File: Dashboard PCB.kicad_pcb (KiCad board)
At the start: 2 copper layers, 62 parts, among them J1 Controls_Leader_Export_02x06, J3 INDICATOR_SWITCH_OUT, J4 FAN_CTRL_01x02, J5 Horn_In_01x02, J6 Horn_Out_01x02

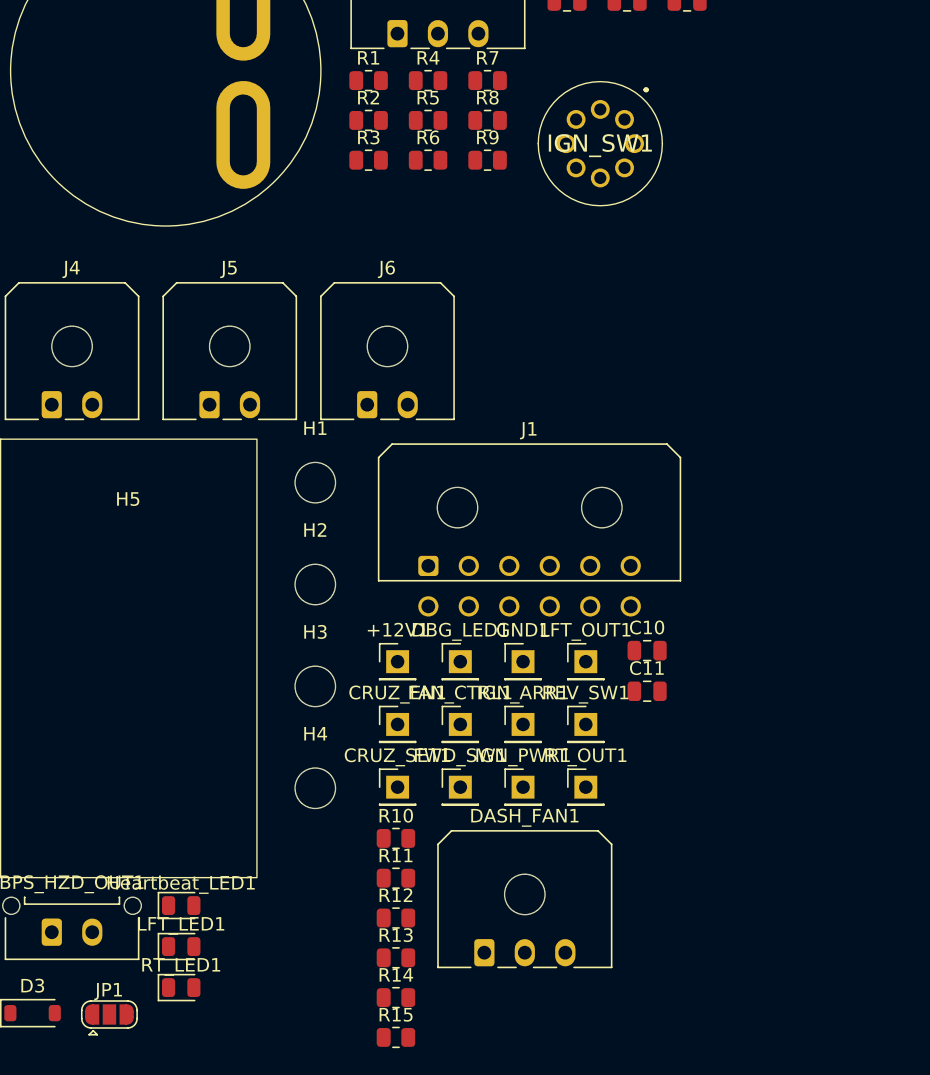
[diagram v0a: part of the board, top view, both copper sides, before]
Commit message: Fixed fan and rot switch
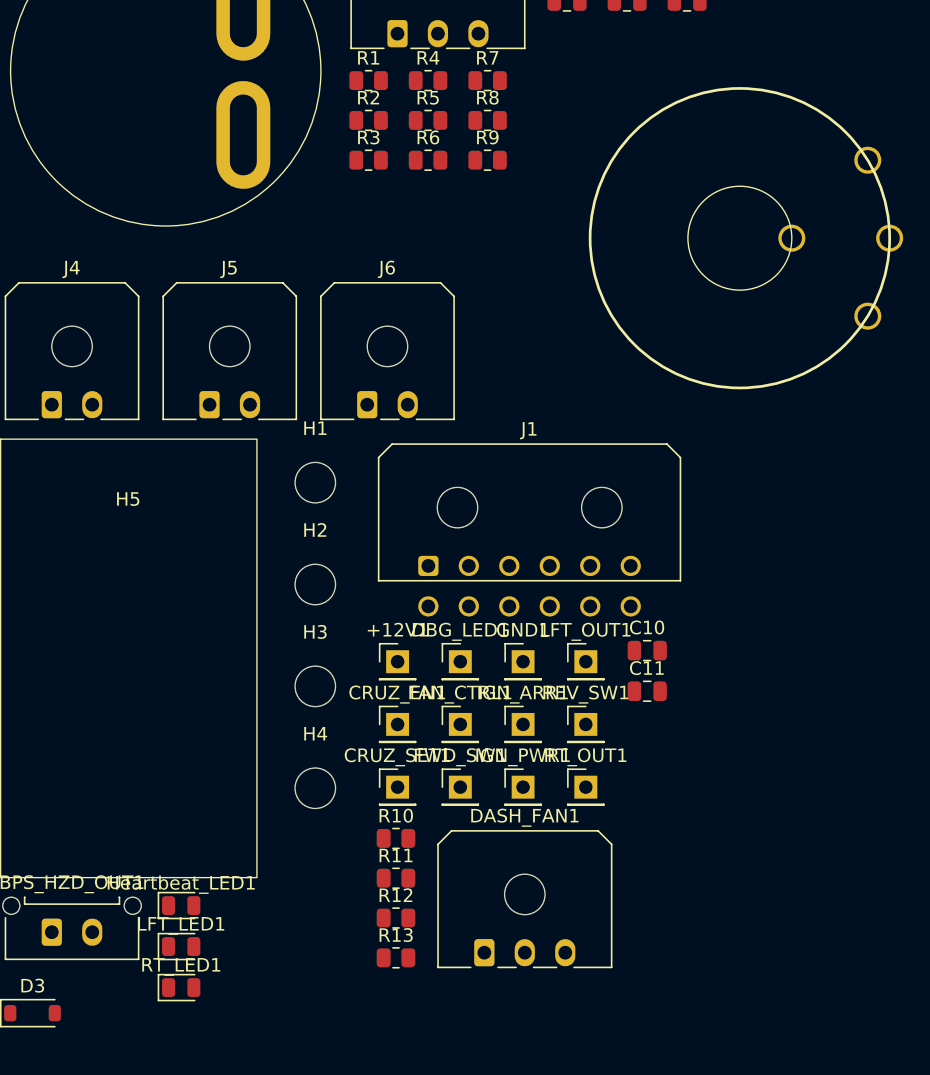
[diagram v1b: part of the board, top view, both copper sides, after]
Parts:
- removed JP1: Jumper_3_Open, Jumper:SolderJumper-3_P1.3mm_Open_RoundedPad1.0x1.5mm
- removed R14: 1.8k, Resistor_SMD:R_0805_2012Metric
- removed R15: 680, Resistor_SMD:R_0805_2012Metric
- DASH_FAN1: value DASHBOARD_FAN_12V+PWM -> DASHBOARD_FAN_12V
- IGN_SW1: footprint switched:SW_ROT_3POS -> switched:SW_3POS_ROT
- moved IGN_SW1 12.3 mm to (72.0, 67.2)
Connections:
- D3 pad 1: +12V -> /FAN+
- D3 pad 2: GND -> /FAN-
- DASH_FAN1 pad 1: +12V -> /FAN+
- DASH_FAN1 pad 2: /FAN_CTRL -> /FAN-
- DASH_FAN1 pad 3: GND -> unconnected-(DASH_FAN1-Pin_3-Pad3)
- FAN_CTRL1 pad 1: /FAN_CTRL -> /FAN+
- IGN_SW1 pad 1: unconnected-(IGN_SW1-Pad1) -> +12V
- J4 pad 1: /FAN_PWM -> /FAN+
- J4 pad 2: GND -> /FAN-

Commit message: Preliminary PCB layout
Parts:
- moved H2 216.3 mm to (246.9, 28.0)
- moved H4 209.4 mm to (246.9, 143.6)
- moved H5 189.2 mm to (215.8, 104.4)
- moved IGN_ARR1 160.8 mm to (212.2, 65.2)
- moved R5 152.7 mm to (199.7, 82.3), turned to 90 degrees
- moved RT_LED1 147.4 mm to (160.8, 53.6)
- moved CRUZ_SET_SW1 146.9 mm to (169.3, 99.7), turned to -90 degrees
- moved R6 136.0 mm to (183.3, 82.5), turned to 90 degrees
- moved LFT_LED1 136.0 mm to (149.4, 53.6), turned to 180 degrees
- moved C5 135.4 mm to (194.2, 82.5), turned to -90 degrees
- moved R11 132.8 mm to (164.8, 54.3), turned to 90 degrees
- moved R8 131.7 mm to (172.0, 115.6), turned to -90 degrees
- moved C6 128.8 mm to (188.2, 82.7), turned to -90 degrees
- moved IGN_PWR1 125.8 mm to (174.2, 65.1)
- moved CRUZ_EN_SW1 124.2 mm to (131.8, 99.5), turned to -90 degrees
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
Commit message: Preliminary schematic
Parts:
- moved R13 140.9 mm to (228.6, 125.1)
- moved BPS_HZD_OUT1 140.7 mm to (227.1, 131.9)
- moved H5 108.7 mm to (116.7, 59.8)
- moved C2 54.9 mm to (69.7, 122.6), turned to 180 degrees
- moved J3 54.6 mm to (76.0, 128.2), turned to 180 degrees
- moved R2 50.8 mm to (69.7, 117.8), turned to 0 degrees
- moved C1 47.3 mm to (76.9, 122.7), turned to 180 degrees
- moved J6 44.9 mm to (89.1, 128.2), turned to 180 degrees
- moved R1 42.5 mm to (77.0, 118.1), turned to 0 degrees
- moved C7 36.1 mm to (149.3, 74.3)
- moved D1 36.1 mm to (148.9, 65.2)
- moved HZD_SW1 36.1 mm to (161.4, 72.2)
- moved R7 36.1 mm to (149.4, 69.2)
- moved D2 36.1 mm to (148.7, 79.6)
- moved H1 35.9 mm to (53.5, 42.6)
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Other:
- board text added: "Controls Export"
- board text added: "Fan Ctrl"
- board text added: "Horn In"
- board text added: "Horn Out"
- board text added: "Indicator Sw Out"

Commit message: r
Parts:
- moved H2 0.82 mm to (243.6, 42.6)
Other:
- board outline added: 200 x 100 mm
- board text added: "20cm x 10cm"
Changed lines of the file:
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@@
 		(tags "capacitor")
 		(property "Reference" "C2"
-			(at 0 -1.68 360)
+			(at 0 -1.68 0)
 			(layer "F.SilkS")
 			(effects
@@
 		)
 		(property "Value" "5uF"
-			(at 0 1.68 360)
+			(at 0 1.68 0)
 			(layer "F.Fab")
 			(effects
@@
 		(tags "connector Molex Micro-Fit_3.0 top entry")
 		(property "Reference" "J6"
-			(at 1.5 -8.1 360)
+			(at 1.5 -8.1 0)
 			(layer "F.SilkS")
 			(effects
@@
 		)
 		(property "Value" "Horn_Out_01x02"
-			(at 1.5 3.22 360)
+			(at 1.5 3.22 0)
 			(layer "F.Fab")
 			(hide yes)
@@
 		(tags "resistor")
 		(property "Reference" "R2"
-			(at 0 -1.65 360)
+			(at 0 -1.65 0)
 			(layer "F.SilkS")
 			(effects
@@
 		)
 		(property "Value" "10k"
-			(at 0 1.65 360)
+			(at 0 1.65 0)
 			(layer "F.Fab")
 			(effects
@@
 		(tags "resistor")
 		(property "Reference" "R13"
-			(at 0 -1.65 360)
+			(at 0 -1.65 0)
 			(layer "F.SilkS")
 			(effects
@@
 		)
 		(property "Value" "HZD_RES_VAL"
-			(at 0 1.65 360)
+			(at 0 1.65 0)
 			(layer "F.Fab")
 			(effects
@@
 		)
 		(fp_text user "${REFERENCE}"
-			(at 0 0 360)
+			(at 0 0 0)
 			(layer "F.Fab")
 			(effects
@@
 	(footprint "MountingHole:MountingHole_3mm"
 		(layer "F.Cu")
-		(at 243.8 41.8)
+		(at 243.6 42.6)
 		(descr "Mounting Hole 3mm, no annular")
 		(tags "mounting hole 3mm no annular")
@@
 		(tags "capacitor")
 		(property "Reference" "C1"
-			(at 0 -1.68 360)
+			(at 0 -1.68 0)
 			(layer "F.SilkS")
 			(effects
@@
 		)
 		(property "Value" "5uF"
-			(at 0 1.68 360)
+			(at 0 1.68 0)
 			(layer "F.Fab")
 			(effects
@@
 		(tags "connector Molex Micro-Fit_3.0 top entry")
 		(property "Reference" "J3"
-			(at 2.6 -8.1 360)
+			(at 2.6 -8.1 0)
 			(layer "F.SilkS")
 			(effects
@@
 		)
 		(property "Value" "INDICATOR_SWITCH_OUT"
-			(at 3 3.22 360)
+			(at 3 3.22 0)
 			(layer "F.Fab")
 			(hide yes)
@@
 		(tags "connector Molex Micro-Fit_3.0 vertical")
 		(property "Reference" "BPS_HZD_OUT1"
-			(at 1.5 -3.67 360)
+			(at 1.5 -3.67 0)
 			(layer "F.SilkS")
 			(effects
@@
 		)
 		(property "Value" "BPS_HAZARD_LIGHT"
-			(at 1.5 4.5 360)
+			(at 1.5 4.5 0)
 			(layer "F.Fab")
 			(effects
@@
 		)
 		(fp_text user "${REFERENCE}"
-			(at 1.5 1.2 360)
+			(at 1.5 1.2 0)
 			(layer "F.Fab")
 			(effects
@@
 		(tags "resistor")
 		(property "Reference" "R1"
-			(at 0 -1.65 360)
+			(at 0 -1.65 0)
 			(layer "F.SilkS")
 			(effects
@@
 		)
 		(property "Value" "10k"
-			(at 0 1.65 360)
+			(at 0 1.65 0)
 			(layer "F.Fab")
 			(effects
@@
 		)
 		(property "Value" "TestPoint"
-			(at 0 2.33 360)
+			(at 0 2.33 0)
 			(layer "F.Fab")
 			(hide yes)
@@
 		)
 		(fill none)
-		(layer "F.Cu")
+		(layer "Edge.Cuts")
+	)
+	(gr_text "20cm x 10cm"
+		(at 45.9 33.4 0)
+		(layer "F.SilkS")
+		(effects
+			(font
+				(size 2 2)
+				(thickness 0.1)
+			)
+			(justify left bottom)
+		)
 	)
 	(gr_text "Controls Export"

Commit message: Changed layout, added 3d models
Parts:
- added J2: CAN, Connector_Molex:Molex_Micro-Fit_3.0_43045-0600_2x03_P3.00mm_Horizontal, B.Cu at (74.0, 104.0)
- added J7: CAN, Connector_Molex:Molex_Micro-Fit_3.0_43045-0600_2x03_P3.00mm_Horizontal, B.Cu at (86.0, 133.0)
- +12V1, BPS_HZD_OUT1, C1, C10, C11, C2, C3, C4, C5, C6, C7, C8, C9, CRUZ_EN1, CRUZ_SET1, D1, D2, D3, DASH_FAN1, DBG_LED1, FAN_CTRL1, FWD_SW1, GND1, Heartbeat_LED1, IGN_ARR1, IGN_PWR1, J1, J3, J4, J5, J6, LFT_OUT1, R1, R10, R11, R12, R13, R2, R3, R4, R5, R6, R7, R8, R9, REV_SW1, RT_OUT1: moved to B.Cu
- CRUZ_EN_SW1, CRUZ_SET_SW1: footprint switched:SW_Butt_) -> Button_Switch_THT:SW_PUSH_6mm
- GR_SW1: footprint switched:SW_100_SP3T-Vertical -> switched:3posSlideToggle
- moved IGN_ARR1 133.0 mm to (93.0, 61.0), turned to 180 degrees
- moved CRUZ_SET1 113.8 mm to (117.0, 49.0), turned to 180 degrees
- moved IGN_PWR1 95.7 mm to (93.0, 55.0), turned to 180 degrees
- moved CRUZ_EN1 86.3 mm to (117.0, 55.0), turned to 180 degrees
- moved FAN_CTRL1 73.3 mm to (101.0, 61.0), turned to -90 degrees
- moved RT_OUT1 56.6 mm to (117.0, 61.0), turned to 180 degrees
- moved LFT_OUT1 50.2 mm to (101.0, 49.0), turned to 180 degrees
- moved REV_SW1 48.7 mm to (109.0, 55.0), turned to 180 degrees
- moved R7 41.6 mm to (189.0, 82.0), turned to 90 degrees
- moved D2 40.4 mm to (189.0, 77.0), turned to -90 degrees
- moved R2 38.9 mm to (107.5, 127.0)
- moved R10 38.4 mm to (189.0, 61.0)
- moved C2 37.8 mm to (107.5, 123.0)
- moved FWD_SW1 37.1 mm to (109.0, 61.0), turned to 180 degrees
- moved LFT_LED1 36.7 mm to (192.0, 58.0)
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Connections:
- BPS_HZD_OUT1 pad 2: GND -> /BPS_HZD
- GR_SW1 pad 1: /FWD_SW -> +12V
- GR_SW1 pad 2: +12V -> /FWD_SW
- GR_SW1 pad 3: /REV_SW -> (no net)
- Heartbeat_LED1 pad 1: GND -> /DBG_LED
- R12 pad 1: /DBG_LED -> +12V
- R13 pad 1: /BPS_HZD -> +12V
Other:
- outline, holes or cut-outs redrawn
- board text added: "Approx 3d model"
- board text added: "Placeholder 3d model"

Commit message: Some extra stuff and things
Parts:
- HZD_SW1: footprint switched:SW_HAZARD -> switched:Toggle
- moved HZD_SW1 2.50 mm to (180.0, 78.5)
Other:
- outline, holes or cut-outs redrawn
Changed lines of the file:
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@@
 		(tags "LED")
 		(property "Reference" "LFT_LED1"
-			(at 0 2 360)
+			(at 0 2 0)
 			(layer "F.SilkS")
 			(effects
@@
 		)
 		(property "Value" "SMD_0805"
-			(at 0 1.65 360)
+			(at 0 1.65 0)
 			(layer "F.Fab")
 			(hide yes)
@@
 		)
 	)
-	(footprint "switched:SW_HAZARD"
+	(footprint "switched:Toggle"
 		(layer "F.Cu")
-		(at 180 81)
+		(at 180 78.5)
 		(property "Reference" "HZD_SW1"
-			(at 0.21 -14.17 0)
+			(at -0.16 7 0)
+			(unlocked yes)
 			(layer "F.SilkS")
-			(hide yes)
 			(effects
 				(font
 					(size 1 1)
-					(thickness 0.15)
+					(thickness 0.1)
 				)
 			)
 		)
 		(property "Value" "HAZARD_SWITCH_12V"
-			(at -0.03 13.54 0)
+			(at 0 9 0)
+			(unlocked yes)
 			(layer "F.Fab")
-			(hide yes)
 			(effects
 				(font
@@
 			)
 		)
-		(property "Footprint" "switched:SW_HAZARD"
-			(at -0.34 -0.31 0)
+		(property "Footprint" "switched:Toggle"
+			(at -0.16 9.85 0)
+			(unlocked yes)
 			(layer "F.Fab")
 			(hide yes)
 			(effects
 				(font
-					(size 1.27 1.27)
+					(size 1 1)
 					(thickness 0.15)
 				)
@@
 		)
 		(property "Datasheet" "https://www.digikey.com/en/products/detail/switch-components/TE1-1A-DC-1-AL/11493057"
-			(at -0.34 -0.31 0)
+			(at -0.16 9.85 0)
+			(unlocked yes)
 			(layer "F.Fab")
 			(hide yes)
 			(effects
 				(font
-					(size 1.27 1.27)
+					(size 1 1)
 					(thickness 0.15)
 				)
@@
 		)
 		(property "Description" "Single Pole Single Throw (SPST) switch"
-			(at -0.34 -0.31 0)
+			(at -0.16 9.85 0)
+			(unlocked yes)
 			(layer "F.Fab")
 			(hide yes)
 			(effects
 				(font
-					(size 1.27 1.27)
+					(size 1 1)
 					(thickness 0.15)
 				)
@@
 		(attr through_hole)
 		(fp_rect
-			(start -7 -12.19)
-			(end 7 12.21)
+			(start -5 -5)
+			(end 5 5)
 			(stroke
 				(width 0.1)
@@
 			(layer "F.SilkS")
 		)
-		(fp_circle
-			(center -5.98 -10.93)
-			(end -5.88 -10.93)
-			(stroke
-				(width 0.2)
-				(type solid)
-			)
-			(fill none)
-			(layer "F.SilkS")
-		)
 		(fp_rect
-			(start -7.15 -12.32)
-			(end 7.16 12.37)
+			(start -5.3 -5.3)
+			(end 5.3 5.3)
 			(stroke
-				(width 0.05)
+				(width 0.1)
 				(type default)
 			)
 			(fill none)
-			(layer "F.CrtYd")
+			(layer "Margin")
 		)
 		(fp_text user "SW_HAZ"
-			(at -2.75 11.49 0)
+			(at -3 1 0)
 			(unlocked yes)
 			(layer "F.SilkS")
@@
 			)
 		)
-		(pad "1" thru_hole rect
-			(at 0 -6.39)
-			(size 9 4)
-			(drill oval 7 2)
+		(fp_text user "${REFERENCE}"
+			(at -0.16 11 0)
+			(unlocked yes)
+			(layer "F.Fab")
+			(effects
+				(font
+					(size 1 1)
+					(thickness 0.15)
+				)
+			)
+		)
+		(pad "1" thru_hole circle
+			(at 2.5 2.5)
+			(size 1.524 1.524)
+			(drill 0.762)
 			(layers "*.Cu" "*.Mask")
 			(remove_unused_layers no)
@@
 			(pinfunction "A")
 			(pintype "passive")
-			(solder_mask_margin 0.102)
 		)
-		(pad "2" thru_hole oval
-			(at 0 0.01)
-			(size 9 4)
-			(drill oval 7 2)
+		(pad "2" thru_hole circle
+			(at 0 2.5)
+			(size 1.524 1.524)
+			(drill 0.762)
 			(layers "*.Cu" "*.Mask")
 			(remove_unused_layers no)
@@
 			(pinfunction "B")
 			(pintype "passive")
-			(solder_mask_margin 0.102)
 		)
-		(pad "3" thru_hole oval
-			(at 0 6.41)
-			(size 9 4)
-			(drill oval 7 2)
+		(pad "3" thru_hole circle
+			(at -2.5 2.5)
+			(size 1.524 1.524)
+			(drill 0.762)
 			(layers "*.Cu" "*.Mask")
 			(remove_unused_layers no)
-			(solder_mask_margin 0.102)
 		)
-		(model "${KIPRJMOD}/3d models/ToggleSwitch 3Pin.step"
+		(pad "4" thru_hole circle
+			(at 2.5 -2.5)
+			(size 1.524 1.524)
+			(drill 0.762)
+			(layers "*.Cu" "*.Mask")
+			(remove_unused_layers no)
+		)
+		(pad "5" thru_hole circle
+			(at 0 -2.5)
+			(size 1.524 1.524)
+			(drill 0.762)
+			(layers "*.Cu" "*.Mask")
+			(remove_unused_layers no)
+		)
+		(pad "6" thru_hole circle
+			(at -2.5 -2.5)
+			(size 1.524 1.524)
+			(drill 0.762)
+			(layers "*.Cu" "*.Mask")
+			(remove_unused_layers no)
+		)
+		(model "${KIPRJMOD}/3d models/ToggleButt.stp"
 			(offset
-				(xyz 0 0 13.5)
+				(xyz 0 0 3.5)
 			)
 			(scale
-				(xyz 1.7 1.4 1.3)
+				(xyz 1 1 1)
 			)
 			(rotate
-				(xyz 0 0 0)
+				(xyz -90 0 90)
 			)
 		)
@@
 		(tags "tact sw push 6mm")
 		(property "Reference" "CRUZ_EN_SW1"
-			(at 3.25 -2.75 360)
+			(at 3.25 -2.75 0)
 			(layer "F.SilkS")
 			(effects
@@
 		)
 		(property "Value" "CRUSE_EN_SW_12V"
-			(at 3.75 6.7 360)
+			(at 3.75 6.7 0)
 			(layer "F.Fab")
 			(effects
@@
 		)
 		(fp_text user "${REFERENCE}"
-			(at 3.25 2.25 360)
+			(at 3.25 2.25 0)
 			(layer "F.Fab")
 			(effects
@@
 		(tags "LED")
 		(property "Reference" "RT_LED1"
-			(at 0 -2 360)
+			(at 0 -2 0)
 			(layer "F.SilkS")
 			(effects
@@
 		)
 		(property "Value" "SMD_0805"
-			(at 0 1.65 360)
+			(at 0 1.65 0)
 			(layer "F.Fab")
 			(hide yes)
@@
 		(tags "capacitor")
 		(property "Reference" "C2"
-			(at 0 1.68 360)
+			(at 0 1.68 0)
 			(layer "B.SilkS")
 			(effects
@@
 		)
 		(property "Value" "5uF"
-			(at 0 -1.68 360)
+			(at 0 -1.68 0)
 			(layer "B.Fab")
 			(effects
@@
 		(tags "resistor")
 		(property "Reference" "R2"
-			(at 0 1.65 360)
+			(at 0 1.65 0)
 			(layer "B.SilkS")
 			(effects
@@
 		)
 		(property "Value" "10k"
-			(at 0 -1.65 360)
+			(at 0 -1.65 0)
 			(layer "B.Fab")
 			(effects
@@
 		(tags "resistor")
 		(property "Reference" "R13"
-			(at 0 2 360)
+			(at 0 2 0)
 			(layer "B.SilkS")
 			(effects
@@
 		)
 		(property "Value" "HZD_RES_VAL"
-			(at 0 -1.65 360)
+			(at 0 -1.65 0)
 			(layer "B.Fab")
 			(effects
@@
 		)
 		(fp_text user "${REFERENCE}"
-			(at 0 -1 360)
+			(at 0 -1 0)
 			(layer "B.Fab")
 			(effects
@@
 		(tags "capacitor")
 		(property "Reference" "C1"
-			(at 0 1.68 360)
+			(at 0 1.68 0)
 			(layer "B.SilkS")
 			(effects
@@
 		)
 		(property "Value" "5uF"
-			(at 0 -1.68 360)
+			(at 0 -1.68 0)
 			(layer "B.Fab")
 			(effects
@@
 		(tags "connector Molex Micro-Fit_3.0 horizontal")
 		(property "Reference" "J7"
-			(at 3 8 360)
+			(at 3 8 0)
 			(layer "B.SilkS")
 			(effects
@@
 		)
 		(fp_text user "${REFERENCE}"
-			(at 3 8.22 360)
+			(at 3 8.22 0)
 			(layer "B.Fab")
 			(effects
@@
 		(tags "connector Molex Micro-Fit_3.0 vertical")
 		(property "Reference" "BPS_HZD_OUT1"
-			(at 1.5 -5 360)
+			(at 1.5 -5 0)
 			(layer "B.SilkS")
 			(effects
@@
 		)
 		(property "Value" "BPS_HAZARD_LIGHT"
-			(at 1.5 -4.5 360)
+			(at 1.5 -4.5 0)
 			(layer "B.Fab")
 			(effects
@@
 		)
 		(fp_text user "${REFERENCE}"
-			(at 1.5 -1.2 360)
+			(at 1.5 -1.2 0)
 			(layer "B.Fab")
 			(effects
@@
 		(tags "resistor")
 		(property "Reference" "R1"
-			(at 0 1.65 360)
+			(at 0 1.65 0)
 			(layer "B.SilkS")
 			(effects
@@
 		)
 		(property "Value" "10k"
-			(at 0 -1.65 360)
+			(at 0 -1.65 0)
 			(layer "B.Fab")
 			(effects
@@
 		(layer "Edge.Cuts")
 	)
-	(gr_arc
-		(start 264 141)
-		(mid 263.414214 142.414214)
-		(end 262 143)
+	(gr_line
+		(start 64 45)
+		(end 64 141)
 		(stroke
-			(width 0.1)
+			(width 0.05)
 			(type default)
 		)
 		(layer "Edge.Cuts")
 	)
-	(gr_rect
-		(start 64 43)
-		(end 264 143)
+	(gr_line
+		(start 262 43)
+		(end 66 43)
 		(stroke
-			(width 0.2)
+			(width 0.05)
+			(type default)
+		)
+		(layer "Edge.Cuts")
+	)
+	(gr_arc
+		(start 264 141)
+		(mid 263.414214 142.414214)
+		(end 262 143)
+		(stroke
+			(width 0.1)
 			(type default)
 		)
-		(fill none)
 		(layer "Edge.Cuts")
 	)
@@
 		(layer "Edge.Cuts")
 	)
+	(gr_line
+		(start 264 141)
+		(end 264 45)
+		(stroke
+			(width 0.05)
+			(type default)
+		)
+		(layer "Edge.Cuts")
+	)
+	(gr_line
+		(start 66 143)
+		(end 262 143)
+		(stroke
+			(width 0.05)
+			(type default)
+		)
+		(layer "Edge.Cuts")
+	)
 	(gr_arc
 		(start 66 143)
@@
 	)
 	(gr_text "Approx\n3d model"
-		(at 135 92 0)
+		(at 134 79 0)
 		(layer "F.Fab")
 		(effects
@@
 		(layer "F.Fab")
 		(effects
-			(font
-				(size 1 1)
-				(thickness 0.1)
-			)
-			(justify left bottom)
-		)
-	)
-	(gr_text "Approx\n3d model"
-		(at 177 97 0)
-		(layer "F.Fab")
-		(effects

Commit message: Fixed stuff
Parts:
- added BPS_HZD: TestPoint, TestPoint:TestPoint_Pad_1.0x1.0mm, B.Cu at (234.0, 139.0)
- +12V: renamed from +12V1; footprint Connector_PinHeader_2.54mm:PinHeader_1x01_P2.54mm_Vertical -> TestPoint:TestPoint_Pad_1.0x1.0mm
- CRUZ_EN: renamed from CRUZ_EN1; footprint Connector_PinHeader_2.54mm:PinHeader_1x01_P2.54mm_Vertical -> TestPoint:TestPoint_Pad_1.0x1.0mm
- CRUZ_SET: renamed from CRUZ_SET1; footprint Connector_PinHeader_2.54mm:PinHeader_1x01_P2.54mm_Vertical -> TestPoint:TestPoint_Pad_1.0x1.0mm
- DBG_LED: renamed from DBG_LED1; footprint Connector_PinHeader_2.54mm:PinHeader_1x01_P2.54mm_Vertical -> TestPoint:TestPoint_Pad_1.0x1.0mm
- FAN_CTRL: renamed from FAN_CTRL1; footprint Connector_PinHeader_2.54mm:PinHeader_1x01_P2.54mm_Vertical -> TestPoint:TestPoint_Pad_1.0x1.0mm
- FWD_SW: renamed from FWD_SW1; footprint Connector_PinHeader_2.54mm:PinHeader_1x01_P2.54mm_Vertical -> TestPoint:TestPoint_Pad_1.0x1.0mm
- GND: renamed from GND1; footprint Connector_PinHeader_2.54mm:PinHeader_1x01_P2.54mm_Vertical -> TestPoint:TestPoint_Pad_1.0x1.0mm
- Heartbeat_LED: renamed from Heartbeat_LED1; moved to F.Cu
- IGN_ARR: renamed from IGN_ARR1; footprint Connector_PinHeader_2.54mm:PinHeader_1x01_P2.54mm_Vertical -> TestPoint:TestPoint_Pad_1.0x1.0mm
- IGN_PWR: renamed from IGN_PWR1; footprint Connector_PinHeader_2.54mm:PinHeader_1x01_P2.54mm_Vertical -> TestPoint:TestPoint_Pad_1.0x1.0mm
- LFT_OUT: renamed from LFT_OUT1; footprint Connector_PinHeader_2.54mm:PinHeader_1x01_P2.54mm_Vertical -> TestPoint:TestPoint_Pad_1.0x1.0mm
- REV_SW: renamed from REV_SW1; footprint Connector_PinHeader_2.54mm:PinHeader_1x01_P2.54mm_Vertical -> TestPoint:TestPoint_Pad_1.0x1.0mm
- RT_OUT: renamed from RT_OUT1; footprint Connector_PinHeader_2.54mm:PinHeader_1x01_P2.54mm_Vertical -> TestPoint:TestPoint_Pad_1.0x1.0mm
- moved IGN_ARR 146.1 mm to (236.0, 91.0)
- moved IGN_PWR 122.3 mm to (211.0, 87.0)
- moved CRUZ_SET 110.0 mm to (201.0, 120.0)
- moved CRUZ_EN 97.0 mm to (189.0, 120.0)
- moved LFT_OUT 85.4 mm to (184.0, 69.0)
- moved REV_SW 76.2 mm to (163.0, 108.8)
- moved FWD_SW 68.3 mm to (163.0, 102.8)
- moved J5 59.5 mm to (99.0, 133.0), turned to 0 degrees
- moved FAN_CTRL 52.1 mm to (83.3, 110.0)
- moved RT_OUT 49.6 mm to (166.0, 69.0)
- moved J7 38.9 mm to (74.0, 96.0), turned to -90 degrees
- moved J4 35.0 mm to (74.0, 126.0)
- moved H5 23.8 mm to (115.0, 81.0)
- moved J2 23.0 mm to (74.0, 81.0)
- moved C10 22.5 mm to (97.0, 62.0), turned to -90 degrees
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- renumbered BPS_HZD_OUT1 to BPS_HZD_OUT, CRUZ_EN_SW1 to CRUZ_EN_SW, CRUZ_SET_SW1 to CRUZ_SET_SW, DASH_FAN1 to DASH_FAN, GR_SW1 to GR_SW, HZD_SW1 to HZD_SW, LFT_LED1 to LFT_LED, RT_LED1 to RT_LED
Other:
- outline, holes or cut-outs redrawn
- board text added: "CAN"
- board text added: "DASH_FAN"
- board text added: "FWD"
- board text added: "IGN_SW"
- board text added: "NUE"
- board text added: "REV"
- board text added: "SUPP_SW"
